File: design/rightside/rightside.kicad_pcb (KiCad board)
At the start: 4 copper layers, 144 x 95.2 mm, 167 parts, among them IC2 XC9148G50CER-G, IC3 nRF52833-QDAA-R7, IC4 74AHCT125PW,118, IC5 MCP23018T-E_SS, IC6 XC9291B33D1R-G, J1 USB_C_Receptacle_USB2.0_16P, J2 Battery Pos, J3 Battery Neg, J4 OLED_128x32, J5 SFV12R-1STBE1HLF, J6 Conn_01x04, U2 BQ24072RGT, U3 USB6B1, U4 BQ27441-G1, U5 PEC11L-4015F-S0015, U6 PEC11L-4015F-S0015, Y1 32 MHz

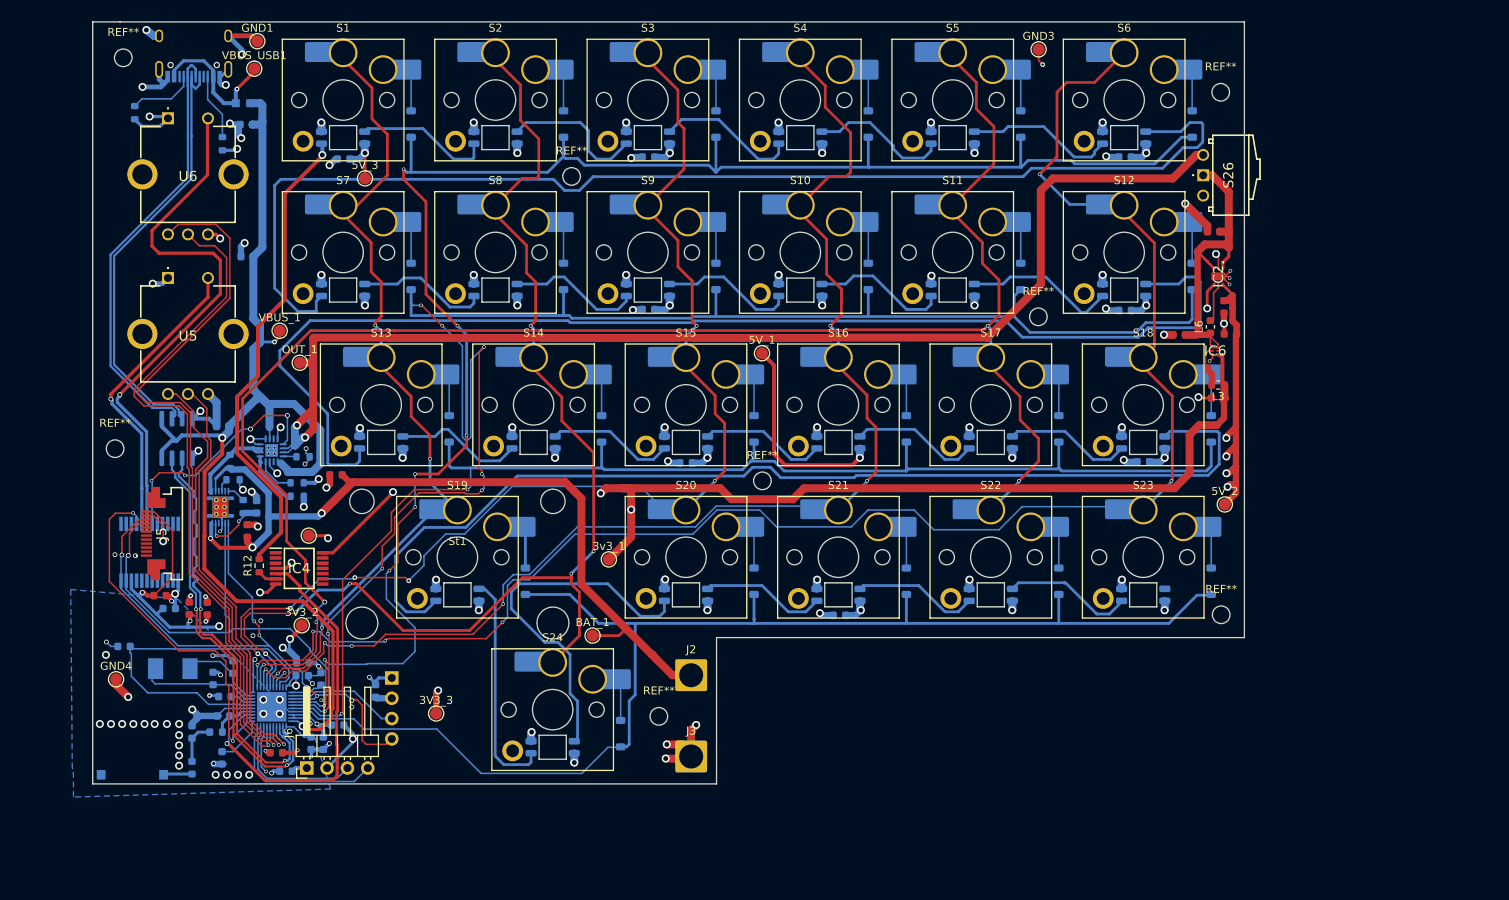
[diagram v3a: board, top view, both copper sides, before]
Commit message: remove old right side routing
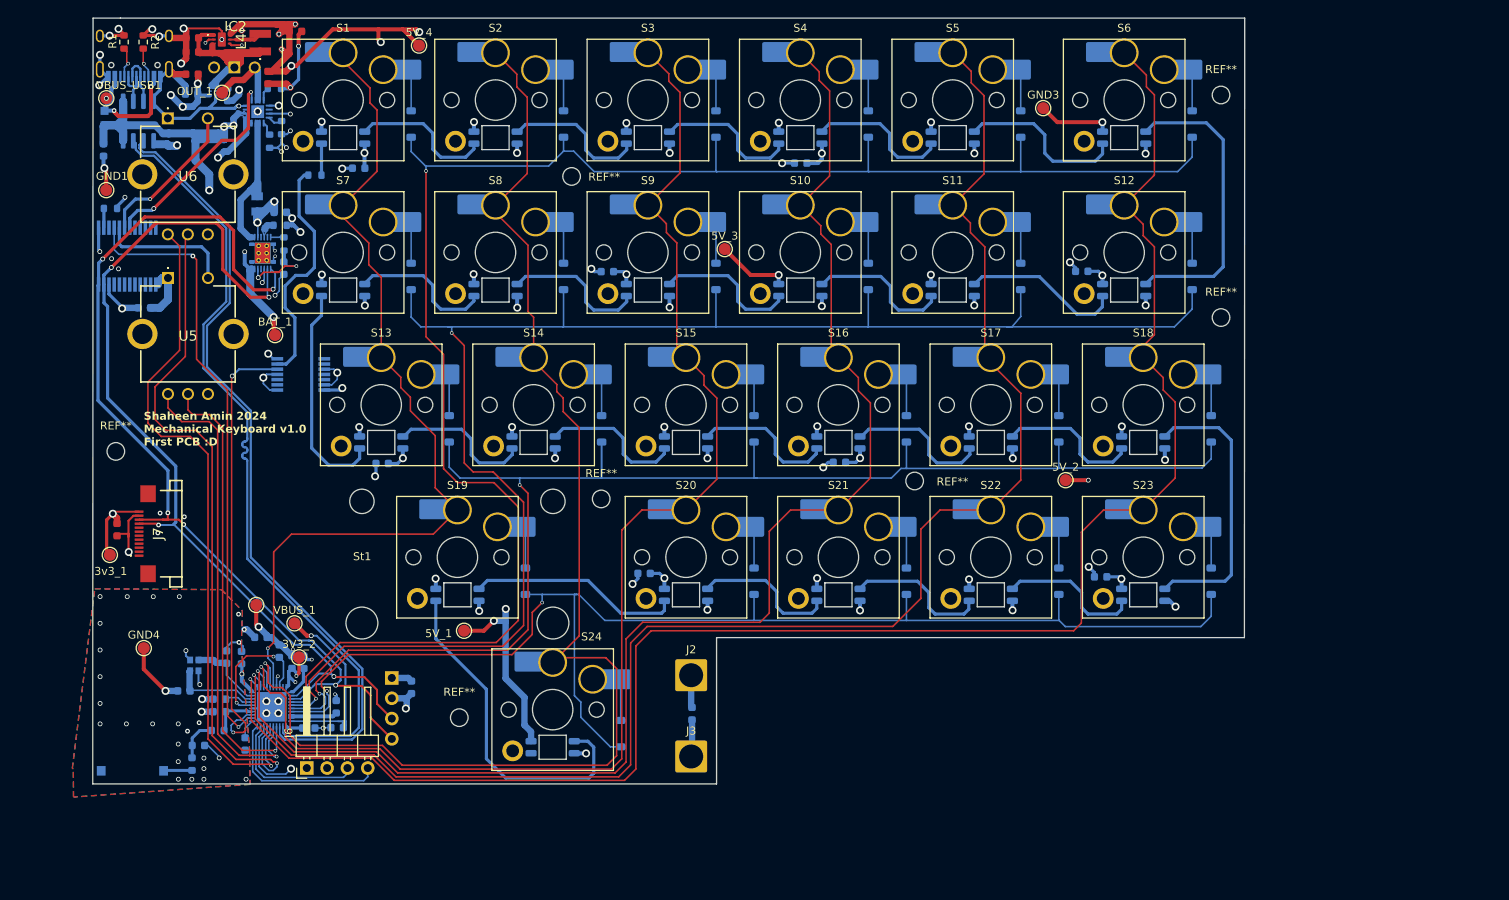
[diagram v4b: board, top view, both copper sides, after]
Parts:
- removed 3V3_3: TestPoint, TestPoint:TestPoint_Pad_D1.5mm
- removed C35, C36, C38, C39: 100nF, ScottoKeebs_Components:Capacitor_0603
- removed J5: SFV12R-1STBE1HLF, SamacSys_Parts:SFV12R1STBE1HLF
- removed L6: 4.7uH, Inductor_SMD:L_0603_1608Metric
- removed R12: 500, Resistor_SMD:R_0603_1608Metric
- removed the REF** at (142.9, 84.1)
- added 5V_4: TestPoint, TestPoint:TestPoint_Pad_D1.5mm, F.Cu at (100.0, 29.7)
- added C40: 100nF, ScottoKeebs_Components:Capacitor_0603, B.Cu at (71.6, 35.8)
- added J7: F32Q-1A7H1-11012, SamacSys_Parts:F32Q1A7H111012, F.Cu at (67.7, 90.7)
- added L4: SRN3015C-4R7M, SamacSys_Parts:SRN3015C4R7M, F.Cu at (80.1, 29.3)
- added R10: 3k, Resistor_SMD:R_0603_1608Metric, B.Cu at (87.0, 45.9)
- added R6: 10m1%, SamacSys_Parts:RESC2012X41N, B.Cu at (79.7, 49.5)
- C17, C18, IC4, IC6, L3, S26: moved to B.Cu
- C26, C27: value 10uF -> 10uF-lowESR
- R1, R2: moved to F.Cu
- R9: value 10m1% -> 10k
- Y1: value 32 MHz -> ECS-320-8-37B2-JTY-TR; footprint SamacSys_Parts:ABM7 -> SamacSys_Parts:ECS320837B2JTYTR
- moved C13 134.4 mm to (71.6, 33.3)
- moved C25 129.6 mm to (71.6, 30.5)
- moved IC6 129.4 mm to (74.2, 35.4), turned to 0 degrees
- moved L3 129.0 mm to (76.1, 35.8), turned to 90 degrees
- moved C10 128.8 mm to (71.6, 28.8)
- moved IC2 128.0 mm to (75.3, 29.0), turned to 0 degrees
- moved C26 122.9 mm to (81.1, 33.7)
- moved C27 122.8 mm to (84.5, 27.9), turned to 0 degrees
- moved S26 121.8 mm to (76.9, 32.4), turned to 0 degrees
- moved C34 100.4 mm to (95.4, 82.0)
- moved 3v3_1 62.4 mm to (61.3, 93.4)
- moved REF** 61.1 mm to (122.8, 86.4)
- moved BAT_1 54.7 mm to (82.0, 65.9)
- moved C17 53.6 mm to (134.1, 113.2), turned to -90 degrees
- moved 5V_1 50.9 mm to (105.6, 102.9)
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- renumbered D9 to D10, D8 to D11, D7 to D12, D23 to D19, D22 to D20, D20 to D22, D19 to D23, D12 to D7, D11 to D8, D10 to D9
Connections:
- net /DEC4 renamed /DEC4_6
- D10 pad 2: Net-(D10-DIN) -> Net-(D10-DOUT)
- D10 pad 4: Net-(D8-DOUT) -> Net-(D10-DIN)
- D11 pad 2: Net-(D8-DOUT) -> Net-(D11-DOUT)
- D11 pad 4: Net-(D7-DOUT) -> Net-(D10-DOUT)
- D12 pad 2: Net-(D7-DOUT) -> Net-(D12-DOUT)
- D12 pad 4: Net-(D6-DOUT) -> Net-(D11-DOUT)
- D19 pad 2: unconnected-(D23-DOUT-Pad2) -> Net-(D19-DOUT)
- D19 pad 4: Net-(D22-DOUT) -> Net-(D18-DOUT)
- D20 pad 2: Net-(D22-DOUT) -> Net-(D20-DOUT)
- D20 pad 4: Net-(D21-DOUT) -> Net-(D19-DOUT)
- D22 pad 2: Net-(D20-DOUT) -> Net-(D22-DOUT)
- D22 pad 4: Net-(D20-DIN) -> Net-(D21-DOUT)
- D23 pad 4: Net-(D18-DOUT) -> Net-(D22-DOUT)
- D24 pad 2: Net-(D20-DIN) -> unconnected-(D24-DOUT-Pad2)
- D7 pad 2: Net-(D12-DOUT) -> Net-(D7-DOUT)
- D7 pad 4: Net-(D11-DOUT) -> Net-(D6-DOUT)
- D8 pad 2: Net-(D11-DOUT) -> Net-(D8-DOUT)
- D8 pad 4: Net-(D10-DOUT) -> Net-(D7-DOUT)
- D9 pad 2: Net-(D10-DOUT) -> Net-(D10-DIN)
- D9 pad 4: Net-(D10-DIN) -> Net-(D8-DOUT)
- IC4 pad 1: unconnected-(IC4-1~{OE}-Pad1) -> GND
- IC4 pad 10: unconnected-(IC4-3~{OE}-Pad10) -> GND
- IC4 pad 13: unconnected-(IC4-4~{OE}-Pad13) -> GND
- IC5 pad 13: unconnected-(IC5-ADDR-Pad13) -> GND
- IC5 pad 14: unconnected-(IC5-~{RESET}-Pad14) -> Net-(IC5-~{RESET})
- R9 pad 1: /BAT -> Net-(IC5-~{RESET})
- R9 pad 2: /BAT_SRN -> 3V3
- Y1 pad 2: Net-(IC3-XC1) -> GND
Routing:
- net 3V3: track 241.7 -> 64.4 mm, vias 15 -> 14
- net /OUT: track 156.8 -> 9.85 mm, vias 2 -> 0
- net Net-(D12-DOUT): track 153.7 -> 28.0 mm
- net Net-(D6-DOUT): track 150.8 -> 37.5 mm
- net Net-(D18-DOUT): track 131.6 -> 35.3 mm
- net /BAT: track 104.3 -> 27.1 mm, vias 3 -> 4
- net /VBUS: track 144.3 -> 74.2 mm, vias 3 -> 5
- net Net-(D1-DIN): track 59.8 -> 3.94 mm, vias 1 -> 0
- net /NO2: track 68.0 -> 19.1 mm
- net /D_N: track 55.1 -> 6.43 mm
- net /D_P: track 55.1 -> 6.52 mm
- net D+: track 52.6 -> 100.7 mm, vias 2 -> 0
- net D-: track 52.6 -> 100.6 mm, vias 2 -> 0
- net /SCL: track 70.7 -> 118.1 mm, vias 1 -> 4
- net Net-(D20-DIN): track 46.1 -> 0.00 mm
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- added copper zone on In1.Cu, net /BAT
- added copper zone on B.Cu, net /VBUS
- added copper zone on In1.Cu, net /VBUS
- added copper zone on F.Cu, net GND
- added copper zone on B.Cu, net Net-(IC3-ANT)
- added copper zone on B.Cu, net Net-(U4-BIN)
- removed copper zone on B.Cu, net D+
- removed copper zone on B.Cu, net D-
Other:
- board size 144 x 95.2 mm -> 144 x 95.7 mm
- board text added: "Shaheen Amin 2024 Mechanical Keyboard v1.0 First PCB :D"

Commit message: restructure for right side and add correct mounting holes
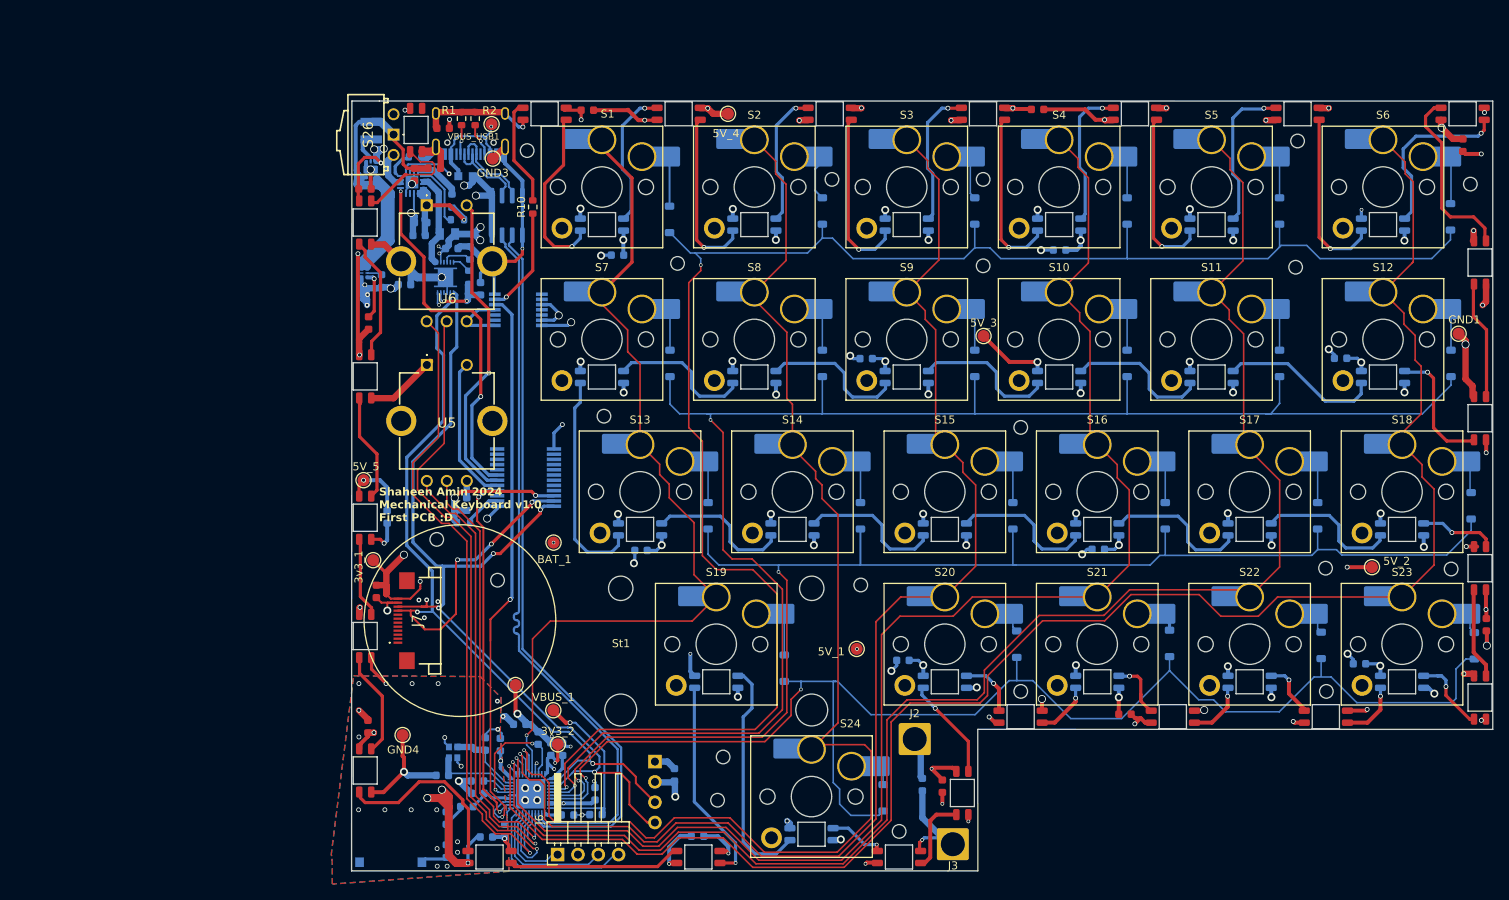
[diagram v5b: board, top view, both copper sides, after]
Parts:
- removed OUT_1: TestPoint, TestPoint:TestPoint_Pad_D1.5mm
- removed the REF** at (161.9, 84.1)
- removed the REF** at (122.8, 86.4)
- removed the REF** at (200.2, 35.9)
- removed the REF** at (105.0, 113.7)
- removed the REF** at (200.2, 63.7)
- removed the REF** at (119.1, 46.1)
- removed the REF** at (62.1, 80.4)
- removed U4: BQ27441-G1, Package_SON:Texas_S-PDSO-N12
- added 5V_5: TestPoint, TestPoint:TestPoint_Pad_D1.5mm, F.Cu at (93.1, 84.0)
- added C35: 100nF, ScottoKeebs_Components:Capacitor_0603, F.Cu at (230.5, 42.2)
- added C36: 100nF, ScottoKeebs_Components:Capacitor_0603, F.Cu at (233.4, 102.1)
- added C38: 100nF, ScottoKeebs_Components:Capacitor_0603, B.Cu at (108.4, 128.6)
- added C39: 100nF, ScottoKeebs_Components:Capacitor_0603, F.Cu at (93.6, 114.8)
- added C41: 100nF, ScottoKeebs_Components:Capacitor_0603, F.Cu at (177.3, 37.7)
- added C42: 100nF, ScottoKeebs_Components:Capacitor_0603, F.Cu at (121.0, 37.8)
- added C43: 100nF, ScottoKeebs_Components:Capacitor_0603, F.Cu at (188.2, 113.3)
- added C44: 10uF, ScottoKeebs_Components:Capacitor_0603, F.Cu at (165.4, 122.3)
- added C45: 100nF, ScottoKeebs_Components:Capacitor_0603, B.Cu at (134.8, 128.5)
- added C46: 100nF, ScottoKeebs_Components:Capacitor_0603, F.Cu at (93.7, 64.4)
- added D25: LED_SK6812MINI, ScottoKeebs_Components:LED_SK6812MINI, B.Cu at (184.8, 90.2)
- added D26: LED_SK6812MINI, ScottoKeebs_Components:LED_SK6812MINI, B.Cu at (203.8, 90.2)
- added D27: LED_SK6812MINI, ScottoKeebs_Components:LED_SK6812MINI, B.Cu at (222.9, 90.2)
- added D28: LED_SK6812MINI, ScottoKeebs_Components:LED_SK6812MINI, F.Cu at (232.6, 95.0)
- added D29: LED_SK6812MINI, ScottoKeebs_Components:LED_SK6812MINI, F.Cu at (232.6, 111.2)
- added D30: LED_SK6812MINI, ScottoKeebs_Components:LED_SK6812MINI, B.Cu at (222.9, 109.2)
- added D31: LED_SK6812MINI, ScottoKeebs_Components:LED_SK6812MINI, F.Cu at (213.3, 113.6)
- added D32: LED_SK6812MINI, ScottoKeebs_Components:LED_SK6812MINI, B.Cu at (203.8, 109.2)
- added D33: LED_SK6812MINI, ScottoKeebs_Components:LED_SK6812MINI, F.Cu at (194.2, 113.6)
- added D34: LED_SK6812MINI, ScottoKeebs_Components:LED_SK6812MINI, B.Cu at (184.8, 109.2)
- added D35: LED_SK6812MINI, ScottoKeebs_Components:LED_SK6812MINI, F.Cu at (175.2, 113.6)
- added D36: LED_SK6812MINI, ScottoKeebs_Components:LED_SK6812MINI, B.Cu at (165.7, 109.2)
- added D37: LED_SK6812MINI, ScottoKeebs_Components:LED_SK6812MINI, F.Cu at (167.9, 123.1)
- added D38: LED_SK6812MINI, ScottoKeebs_Components:LED_SK6812MINI, F.Cu at (160.0, 131.1)
- added D39: LED_SK6812MINI, ScottoKeebs_Components:LED_SK6812MINI, B.Cu at (149.0, 128.3)
- added D40: LED_SK6812MINI, ScottoKeebs_Components:LED_SK6812MINI, B.Cu at (137.1, 109.2)
- added D41: LED_SK6812MINI, ScottoKeebs_Components:LED_SK6812MINI, F.Cu at (134.9, 131.1)
- added D42: LED_SK6812MINI, ScottoKeebs_Components:LED_SK6812MINI, F.Cu at (108.8, 131.1)
- added D43: LED_SK6812MINI, ScottoKeebs_Components:LED_SK6812MINI, F.Cu at (93.3, 120.3)
- added D44: LED_SK6812MINI, ScottoKeebs_Components:LED_SK6812MINI, F.Cu at (93.3, 103.5)
- added D45: LED_SK6812MINI, ScottoKeebs_Components:LED_SK6812MINI, F.Cu at (93.3, 88.7)
- added D46: LED_SK6812MINI, ScottoKeebs_Components:LED_SK6812MINI, F.Cu at (93.3, 71.1)
- added D47: LED_SK6812MINI, ScottoKeebs_Components:LED_SK6812MINI, F.Cu at (93.3, 51.8)
- added D48: LED_SK6812MINI, ScottoKeebs_Components:LED_SK6812MINI, F.Cu at (99.6, 40.3)
- added REF**: M1.6 Hole, CustomLibrary:M1.6 Hole, F.Cu at (209.6, 57.4)
- added REF**: M1.6 Hole, CustomLibrary:M1.6 Hole, F.Cu at (229.0, 95.1)
- added REF**: M1.6 Hole, CustomLibrary:M1.6 Hole, F.Cu at (151.6, 46.4)
- added REF**: M1.6 Hole, CustomLibrary:M1.6 Hole, F.Cu at (170.5, 46.4)
- added REF**: M1.6 Hole, CustomLibrary:M1.6 Hole, F.Cu at (138.0, 118.6)
- added REF**: M1.6 Hole, CustomLibrary:M1.6 Hole, F.Cu at (113.5, 42.8)
- added REF**: M1.6 Hole, CustomLibrary:M1.6 Hole, F.Cu at (137.3, 124.0)
- added REF**: M1.6 Hole, CustomLibrary:M1.6 Hole, F.Cu at (213.4, 110.4)
- added REF**: M1.6 Hole, CustomLibrary:M1.6 Hole, F.Cu at (160.0, 127.9)
- added REF**: M1.6 Hole, CustomLibrary:M1.6 Hole, F.Cu at (123.1, 76.0)
- added REF**: M1.6 Hole, CustomLibrary:M1.6 Hole, F.Cu at (109.8, 96.5)
- added REF**: M1.6 Hole, CustomLibrary:M1.6 Hole, F.Cu at (170.5, 57.2)
- added REF**: M1.6 Hole, CustomLibrary:M1.6 Hole, F.Cu at (175.2, 110.4)
- added REF**: M1.6 Hole, CustomLibrary:M1.6 Hole, F.Cu at (231.4, 47.0)
- added REF**: M1.6 Hole, CustomLibrary:M1.6 Hole, F.Cu at (209.8, 41.6)
- added REF**: M1.6 Hole, CustomLibrary:M1.6 Hole, F.Cu at (132.3, 56.9)
- added REF**: M1.6 Hole, CustomLibrary:M1.6 Hole, F.Cu at (175.2, 77.4)
- added REF**: M1.6 Hole, CustomLibrary:M1.6 Hole, F.Cu at (213.3, 95.0)
- added REF**: M1.6 Hole, CustomLibrary:M1.6 Hole, F.Cu at (155.2, 97.1)
- added REF**: M1.6 Hole, CustomLibrary:M1.6 Hole, F.Cu at (102.2, 91.4)
- added U1: BQ27441-G1, Package_SON:Texas_S-PDSO-N12, B.Cu at (103.3, 58.7)
- C13, IC2, L4: moved to B.Cu
- D1, D11, D13, D14, D15, D3, D5, D7, D9, R10, S26: moved to F.Cu
- moved GND1 170.0 mm to (229.9, 65.7)
- moved D13 141.3 mm to (230.4, 38.2), turned to 180 degrees
- moved D12 130.2 mm to (220.5, 52.1), turned to 0 degrees
- moved D14 120.4 mm to (232.6, 56.8), turned to -90 degrees
- moved D11 102.6 mm to (209.8, 38.2), turned to 0 degrees
- moved D15 99.3 mm to (232.6, 76.3), turned to -90 degrees
- moved D10 70.9 mm to (199.1, 52.1), turned to 0 degrees
- moved GND3 69.1 mm to (109.2, 43.8)
- moved D16 68.6 mm to (220.5, 71.1), turned to 180 degrees
- moved R9 59.1 mm to (105.6, 89.3), turned to 180 degrees
- moved C40 58.2 mm to (96.0, 88.6), turned to 90 degrees
- moved IC5 57.0 mm to (113.3, 83.7), turned to 180 degrees
- moved D24 56.1 mm to (165.7, 90.2), turned to 0 degrees
- moved 5V_1 49.1 mm to (154.7, 105.1)
- moved VBUS_USB1 48.3 mm to (109.1, 39.5)
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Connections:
- C22 pad 1: Net-(U4-V_{DD}) -> Net-(U1-V_{DD})
- C40 pad 2: 3V3 -> 5V
- D24 pad 2: unconnected-(D24-DOUT-Pad2) -> Net-(D24-DOUT)
- R7 pad 1: Net-(U4-BIN) -> GND
- R7 pad 2: GND -> Net-(U1-BIN)
- R8 pad 1: Net-(U4-GPOUT) -> Net-(U1-V_{DD})
- R8 pad 2: Net-(U4-V_{DD}) -> Net-(U1-GPOUT)
- U6 pad MH1: unconnected-(U6-PadMH1) -> GND
- U6 pad MH2: unconnected-(U6-PadMH2) -> GND
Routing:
- net GND: track 230.5 -> 323.4 mm, vias 110 -> 97
- net 5V: track 131.4 -> 168.8 mm, vias 35 -> 58
- net /INTA: track 76.3 -> 45.0 mm
- net Net-(D39-DOUT): track 0.00 -> 29.5 mm
- net Net-(IC2-BAT): track 37.0 -> 63.1 mm
- net Net-(D40-DOUT): track 0.00 -> 26.0 mm, vias 0 -> 1
- net Net-(D23-DOUT): track 43.0 -> 18.1 mm
- net 3V3: track 64.4 -> 88.1 mm
- net /VBUS: track 74.2 -> 50.5 mm
- net Net-(D42-DOUT): track 0.00 -> 22.5 mm
- net Net-(D41-DOUT): track 0.00 -> 21.7 mm
- net /NO2: track 19.1 -> 39.1 mm
- net Net-(D6-DOUT): track 37.5 -> 17.4 mm, vias 0 -> 1
- net /CHG: track 26.5 -> 45.4 mm
- net Net-(D25-DOUT): track 0.00 -> 18.1 mm
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- removed copper zone on B.Cu, net /VBUS
- removed copper zone on B.Cu, net Net-(U4-BIN)
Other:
- board size 144 x 95.7 mm -> 142.6 x 96.2 mm
